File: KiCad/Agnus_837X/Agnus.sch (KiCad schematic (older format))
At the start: 9 parts, among them U3 SN74CBTD16210, U4 SN74CBTD16210, U5 SN74CBTD16210, U6 SN74CBTD16210, U7 Agnus_8375_MB_socket

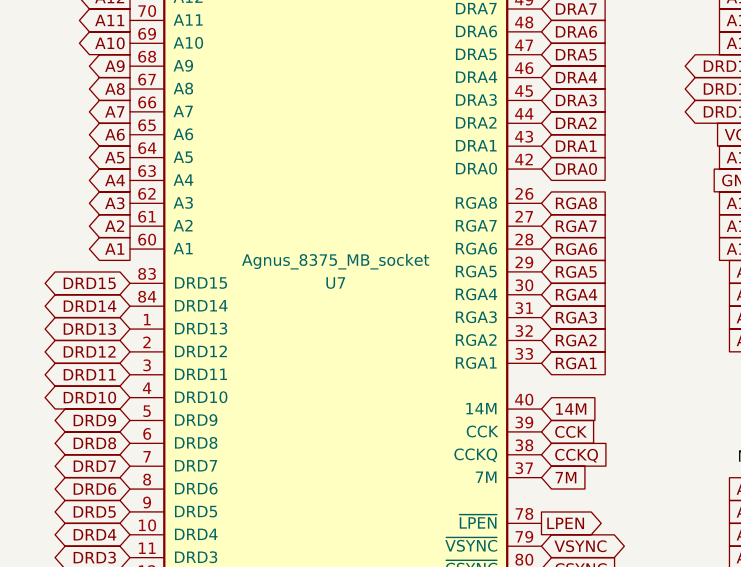
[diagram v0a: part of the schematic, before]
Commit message: small fixes, improved grounding for U5, re-labeled buffer chip to U7, silkscreen fix
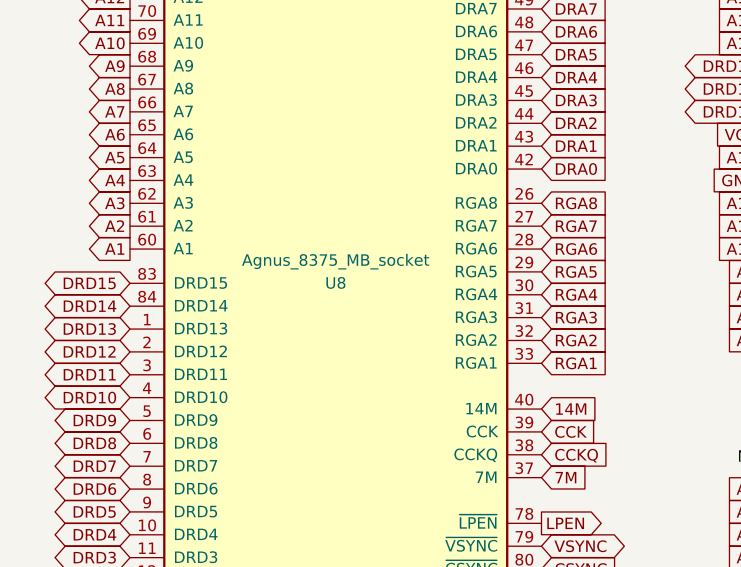
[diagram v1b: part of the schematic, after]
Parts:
- renumbered U7 to U8
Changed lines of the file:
@@
 Connection ~ 2850 6800
 $Comp
-L Agnus:Agnus_8375_socket U7
+L Agnus:Agnus_8375_socket U8
 U 1 1 6061C6CA
 P 1950 3350
-F 0 "U7" H 1950 3450 50  0000 C CNN
+F 0 "U8" H 1950 3450 50  0000 C CNN
 F 1 "Agnus_8375_MB_socket" H 1950 3550 50  0000 C CNN
 F 2 "Agnus:Agnus_30.1x30.1mm_P1.27mm_for_edge_plating" H 2350 5650 50  0001 L CIN

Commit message: switched to footprint made for castellated holes
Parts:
- U8: footprint Agnus:Agnus_30.1x30.1mm_P1.27mm_for_edge_plating -> Agnus:Agnus_30.1x30.1mm_P1.27mm_for_castellated_holes
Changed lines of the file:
@@
 F 0 "U8" H 1950 3450 50  0000 C CNN
 F 1 "Agnus_8375_MB_socket" H 1950 3550 50  0000 C CNN
-F 2 "Agnus:Agnus_30.1x30.1mm_P1.27mm_for_edge_plating" H 2350 5650 50  0001 L CIN
+F 2 "Agnus:Agnus_30.1x30.1mm_P1.27mm_for_castellated_holes" H 2350 5650 50  0001 L CIN
 F 3 "" H 1950 3350 50  0001 C CNN
 	1    1950 3350

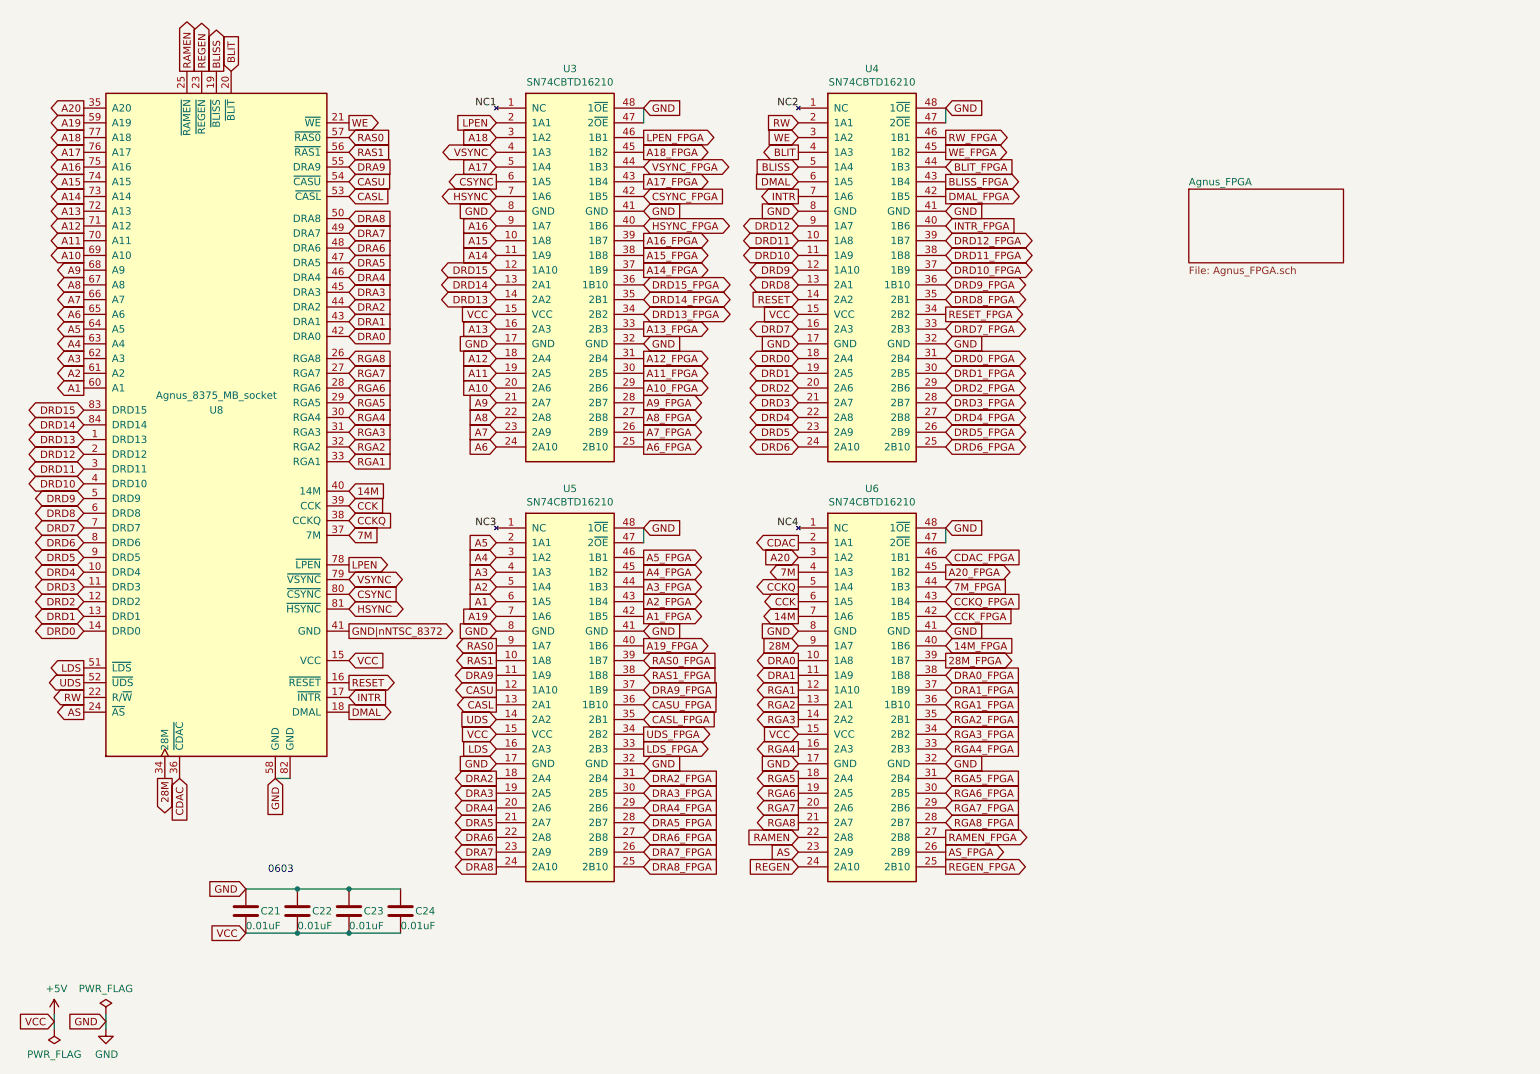
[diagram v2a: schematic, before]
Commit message: Updated design to accommodate a PLCC-84-plug
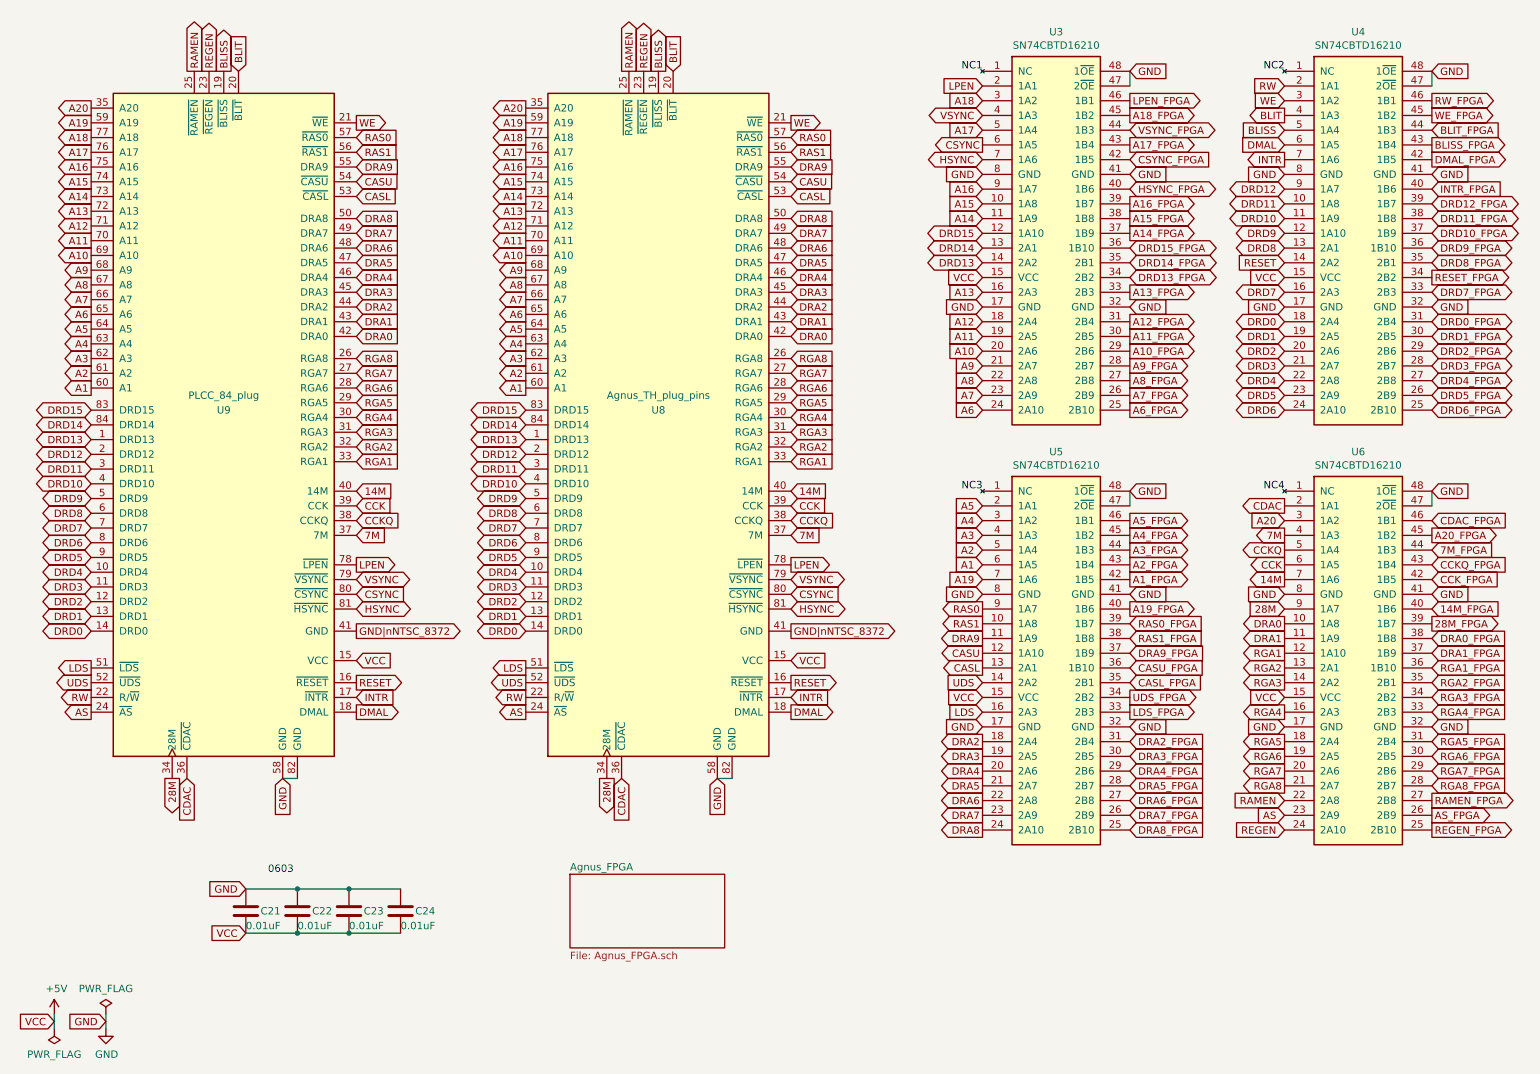
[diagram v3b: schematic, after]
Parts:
- added U9: PLCC_84_plug, Agnus:PLCC-84_Plug_P1.27mm_mirrored, symbol Agnus:Agnus_8375_socket
- U3, U4, U5, U6: footprint Agnus:TSSOP-48_6.1x12.5mm_P0.5mm_padLength_0.8mm -> Agnus:TSSOP-48_6.1x12.5mm_P0.5mm_padLength_1mm
- U8: value Agnus_8375_MB_socket -> Agnus_TH_plug_pins; footprint Agnus:Agnus_30.1x30.1mm_P1.27mm_for_castellated_holes -> Agnus:PLCC-84_TH_pin_holes
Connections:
- net +5V: now also U9.15 (VCC)
- net 14M: now also U9.40 (14M)
- net 28M: now also U9.34 (28M)
- net 7M: now also U9.37 (7M)
- net A1: now also U9.60 (A1)
- net A10: now also U9.69 (A10)
- net A11: now also U9.70 (A11)
- net A12: now also U9.71 (A12)
- net A13: now also U9.72 (A13)
- net A14: now also U9.73 (A14)
- net A15: now also U9.74 (A15)
- net A16: now also U9.75 (A16)
- net A17: now also U9.76 (A17)
- net A18: now also U9.77 (A18)
- net A19: now also U9.59 (A19)
- net A2: now also U9.61 (A2)
- net A20: now also U9.35 (A20)
- net A3: now also U9.62 (A3)
- net A4: now also U9.63 (A4)
- net A5: now also U9.64 (A5)
- net A6: now also U9.65 (A6)
- net A7: now also U9.66 (A7)
- net A8: now also U9.67 (A8)
- net A9: now also U9.68 (A9)
- net AS: now also U9.24 (~AS)
- net BLISS: now also U9.19 (~BLISS)
- net BLIT: now also U9.20 (~BLIT)
- net CASL: now also U9.53 (~CASL)
- net CASU: now also U9.54 (~CASU)
- net CCK: now also U9.39 (CCK)
- net CCKQ: now also U9.38 (CCKQ)
- net CDAC: now also U9.36 (~CDAC)
- net CSYNC: now also U9.80 (~CSYNC)
- net DMAL: now also U9.18 (DMAL)
- net DRA0: now also U9.42 (DRA0)
- net DRA1: now also U9.43 (DRA1)
- net DRA2: now also U9.44 (DRA2)
- net DRA3: now also U9.45 (DRA3)
- net DRA4: now also U9.46 (DRA4)
- net DRA5: now also U9.47 (DRA5)
- net DRA6: now also U9.48 (DRA6)
- net DRA7: now also U9.49 (DRA7)
- net DRA8: now also U9.50 (DRA8)
- net DRA9: now also U9.55 (DRA9)
- net DRD0: now also U9.14 (DRD0)
- net DRD1: now also U9.13 (DRD1)
- net DRD10: now also U9.4 (DRD10)
- net DRD11: now also U9.3 (DRD11)
- net DRD12: now also U9.2 (DRD12)
- net DRD13: now also U9.1 (DRD13)
- net DRD14: now also U9.84 (DRD14)
- net DRD15: now also U9.83 (DRD15)
- net DRD2: now also U9.12 (DRD2)
- net DRD3: now also U9.11 (DRD3)
- net DRD4: now also U9.10 (DRD4)
- net DRD5: now also U9.9 (DRD5)
- net DRD6: now also U9.8 (DRD6)
- net DRD7: now also U9.7 (DRD7)
- net DRD8: now also U9.6 (DRD8)
- net DRD9: now also U9.5 (DRD9)
- net GND: now also U9.58 (GND), U9.82 (GND)
- net GND|nNTSC_8372: now also U9.41 (GND)
- net HSYNC: now also U9.81 (~HSYNC)
- net INTR: now also U9.17 (~INTR)
- net LDS: now also U9.51 (~LDS)
- net LPEN: now also U9.78 (~LPEN)
- net RAMEN: now also U9.25 (~RAMEN)
- net RAS0: now also U9.57 (~RAS0)
- net RAS1: now also U9.56 (~RAS1)
- net REGEN: now also U9.23 (~REGEN)
- net RESET: now also U9.16 (~RESET)
- net RGA1: now also U9.33 (RGA1)
- net RGA2: now also U9.32 (RGA2)
- net RGA3: now also U9.31 (RGA3)
- net RGA4: now also U9.30 (RGA4)
- net RGA5: now also U9.29 (RGA5)
- net RGA6: now also U9.28 (RGA6)
- net RGA7: now also U9.27 (RGA7)
- net RGA8: now also U9.26 (RGA8)
- net RW: now also U9.22 (R/~W)
- net UDS: now also U9.52 (~UDS)
- net VSYNC: now also U9.79 (~VSYNC)
- net WE: now also U9.21 (~WE)
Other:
- moved on the sheet: U3, U4, U5, U6, U8

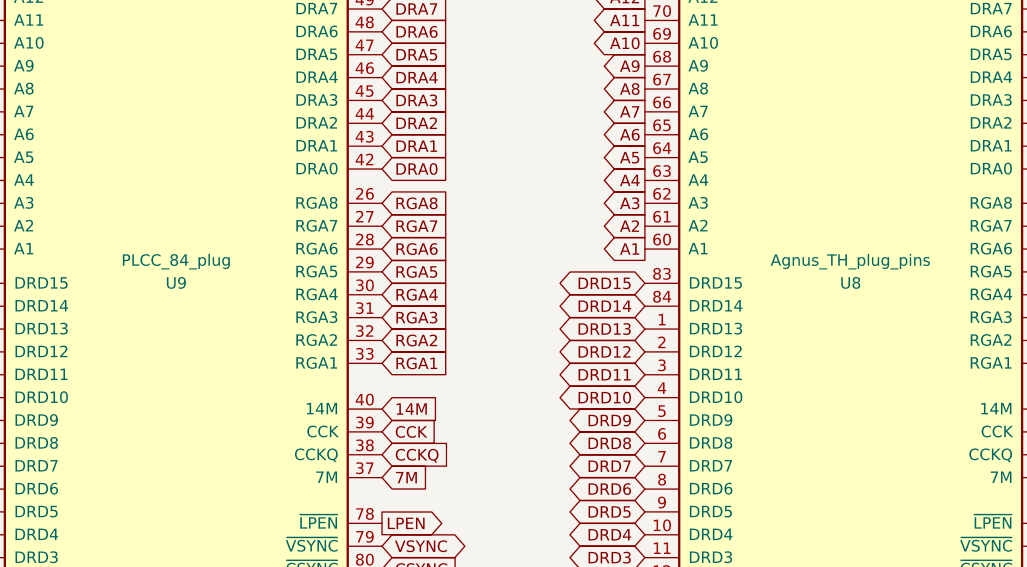
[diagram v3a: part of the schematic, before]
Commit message: Corrected values for capacitors C4,C5,C8,C11 to 1uF and the reference for the Winslow plug to U8 to match the BOM
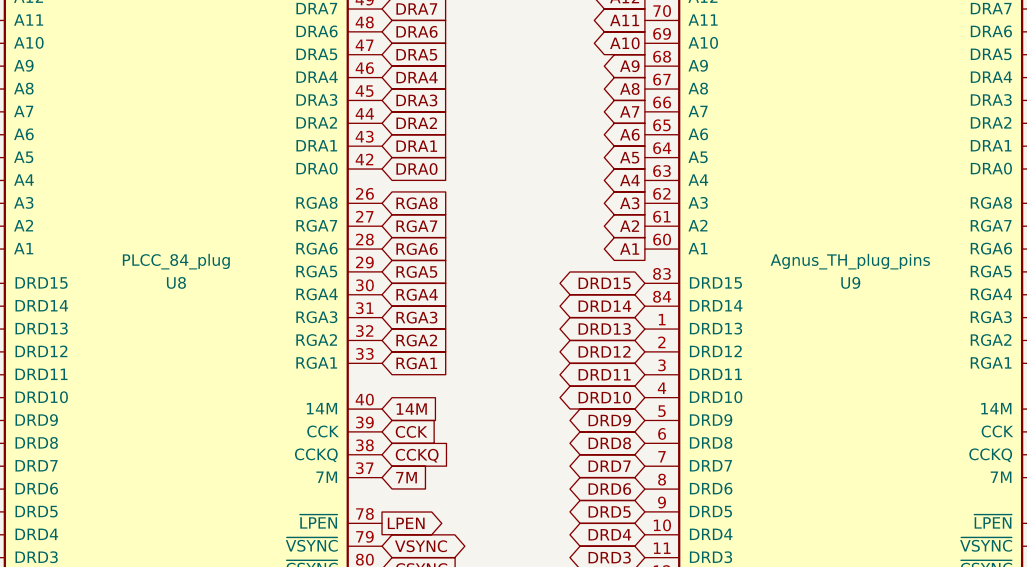
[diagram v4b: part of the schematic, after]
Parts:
- renumbered U9 to U8, U8 to U9
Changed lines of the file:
@@
 Connection ~ 2850 6800
 $Comp
-L Agnus:Agnus_8375_socket U8
+L Agnus:Agnus_8375_socket U9
 U 1 1 6061C6CA
 P 4950 3350
-F 0 "U8" H 4950 3450 50  0000 C CNN
+F 0 "U9" H 4950 3450 50  0000 C CNN
 F 1 "Agnus_TH_plug_pins" H 4950 3550 50  0000 C CNN
 F 2 "Agnus:PLCC-84_TH_pin_holes" H 5350 5650 50  0001 L CIN
@@
 DMAL
 $Comp
-L Agnus:Agnus_8375_socket U9
+L Agnus:Agnus_8375_socket U8
 U 1 1 6519BFAF
 P 2000 3350
-F 0 "U9" H 2000 3450 50  0000 C CNN
+F 0 "U8" H 2000 3450 50  0000 C CNN
 F 1 "PLCC_84_plug" H 2000 3550 50  0000 C CNN
 F 2 "Agnus:PLCC-84_Plug_P1.27mm_mirrored" H 2400 5650 50  0001 L CIN
